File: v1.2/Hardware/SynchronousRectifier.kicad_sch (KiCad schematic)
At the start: 22 parts, among them J1 MAINS_IN, Q21 BC817, Q22 BC817, U1 4N39, U2 4N39

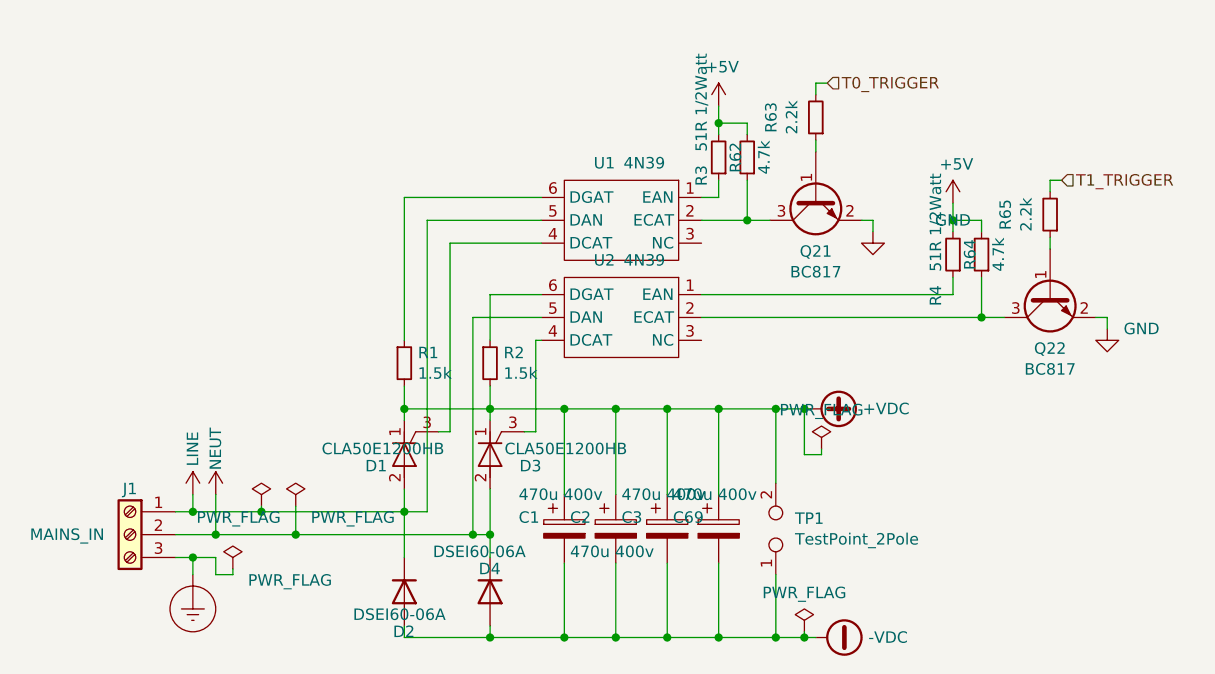
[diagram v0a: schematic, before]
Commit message: Addition of firmware to v1.2(not tested)
+Addition of power tracking(with duty cycle control).
+Addition of resonance freq tracking(via proprietary algorithm relied on active and reactive power measurements)
+Quality factor monitoring
+Power boost when loaded(idle and loaded modes)
+Much better frequency resolution(less than 1Hz)
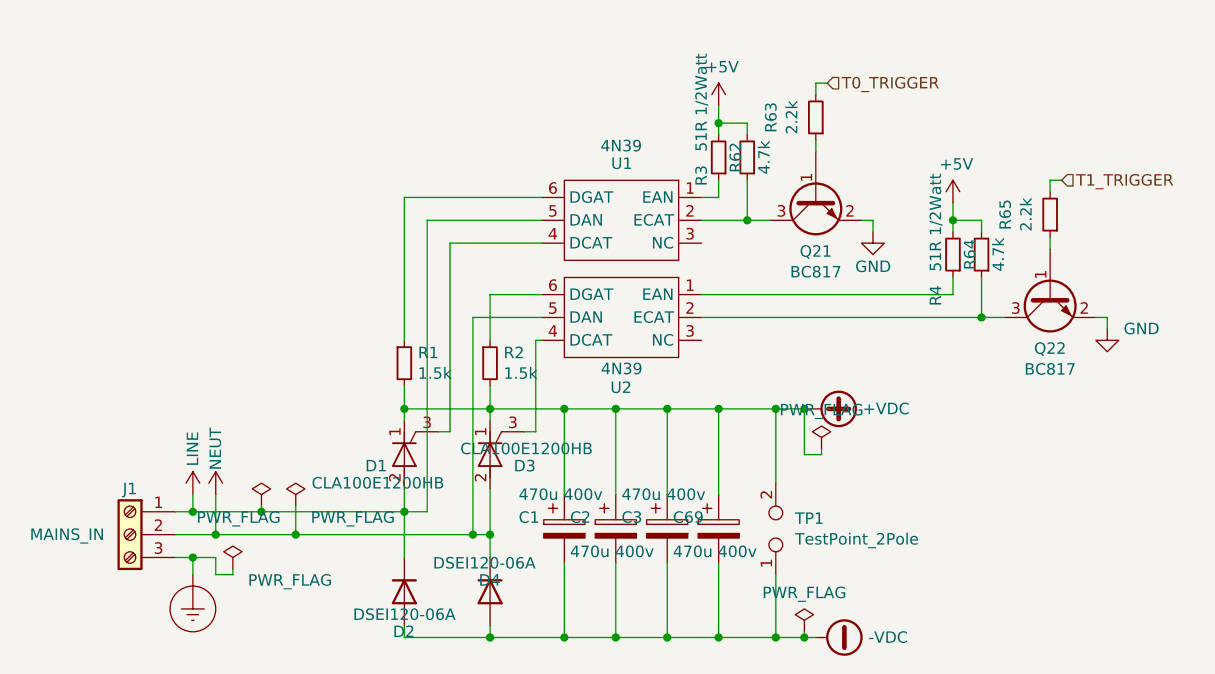
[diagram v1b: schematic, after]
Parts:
- D1, D3: value CLA50E1200HB -> CLA100E1200HB; Link https://ozdisan.com/power-semiconductors/thyristors/discret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 -> https://ozdisan.com/Product/Detail/458855/CLA100E1200HB; Price 13.43667TL -> 29.10196TL
- D2, D4: value DSEI60-06A -> DSEI120-06A; Link https://ozdisan.com/power-semiconductors/diodes-diode-modules-and-rectifiers/general-purpose-diodes/DSEI60-06A -> https://ozdisan.com/power-semiconductors/diodes-diode-modules-and-rectifiers/general-purpose-diodes/DSEI120-06A; Price 20.69234TL -> 47.67769

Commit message: Start of rs485 communication interface development.
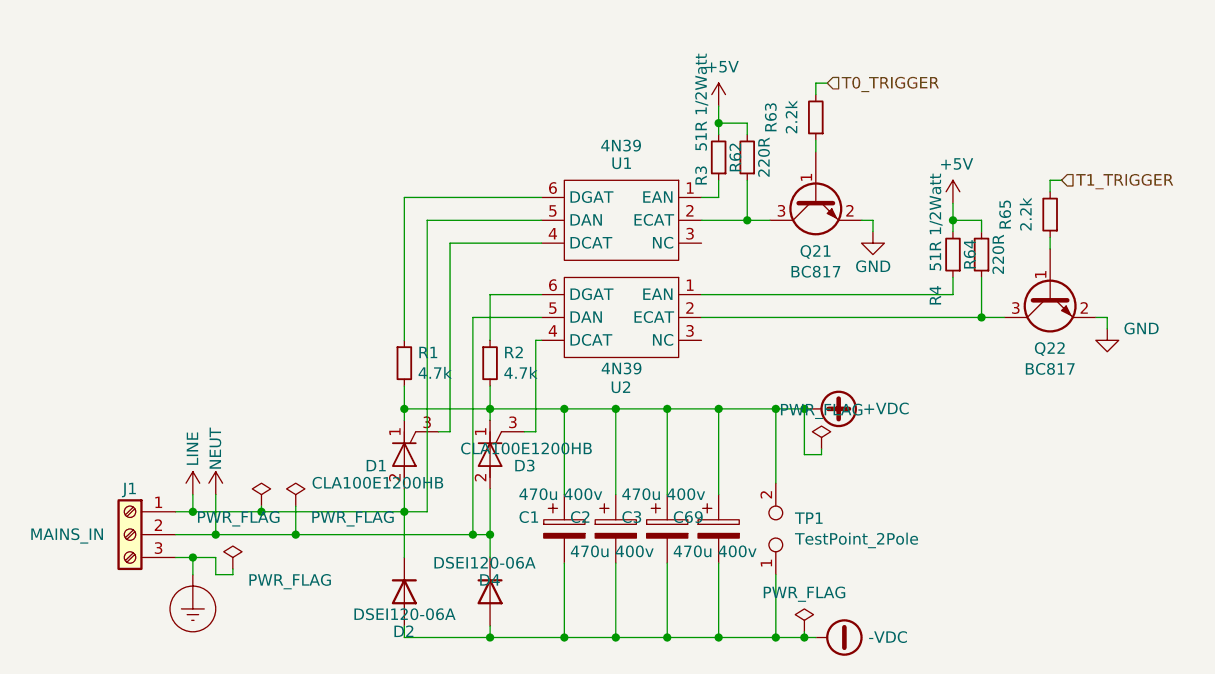
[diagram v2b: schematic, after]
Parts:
- R1, R2: value 1.5k -> 4.7k; Link https://ozdisan.com/passive-components/resistors/tht-through-hole-resistors/CFR0W8J0152A50 -> https://ozdisan.com/passive-components/resistors/tht-through-hole-resistors/CFR0W8J0472A50; Price 0.01961TL -> 0.0389TL
- R62, R64: value 4.7k -> 220R; Link https://ozdisan.com/passive-components/resistors/smt-smd-and-chip-resistors/0805S8F4701T5E -> https://ozdisan.com/passive-components/resistors/smt-smd-and-chip-resistors/0805S8J0221T5E; Price 0.01955TL -> 0.01498TL
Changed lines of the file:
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@@
 (kicad_sch (version 20200618) (host eeschema "5.99.0-unknown-f3f1740~101~ubuntu18.04.1")
-  (page 9 8)
+  (page 4 8)
   (paper "A4")
   (junction (at 99.06 106.68) (diameter 0) (color 0 0 0 0))
@@
     )
   )
-  (symbol (lib_name "Device:R_Small_3") (lib_id "Device:R_Small") (at 122.555 90.17 0)
+  (symbol (lib_name "Device:R_Small_9") (lib_id "Device:R_Small") (at 122.555 90.17 0)
     (in_bom yes) (on_board yes)
     (property "Reference" "R1" (id 0) (at 124.0536 89.027 0)
       (effects (font (size 1.27 1.27)) (justify left))
     )
-    (property "Value" "1.5k" (id 1) (at 124.0536 91.313 0)
+    (property "Value" "4.7k" (id 1) (at 124.0536 91.313 0)
       (effects (font (size 1.27 1.27)) (justify left))
     )
@@
       (effects (font (size 1.27 1.27)) hide)
     )
-    (property "Link" "https://ozdisan.com/passive-components/resistors/tht-through-hole-resistors/CFR0W8J0152A50" (id 4) (at 122.555 90.17 0)
-      (effects (font (size 1.27 1.27)) hide)
-    )
-    (property "Price" "0.01961TL" (id 5) (at 122.555 90.17 0)
-      (effects (font (size 1.27 1.27)) hide)
-    )
-  )
-  (symbol (lib_name "Device:R_Small_2") (lib_id "Device:R_Small") (at 132.08 90.17 0)
+    (property "Link" "https://ozdisan.com/passive-components/resistors/tht-through-hole-resistors/CFR0W8J0472A50" (id 4) (at 122.555 90.17 0)
+      (effects (font (size 1.27 1.27)) hide)
+    )
+    (property "Price" "0.0389TL" (id 5) (at 122.555 90.17 0)
+      (effects (font (size 1.27 1.27)) hide)
+    )
+  )
+  (symbol (lib_name "Device:R_Small_9") (lib_id "Device:R_Small") (at 132.08 90.17 0) (unit 1)
     (in_bom yes) (on_board yes)
     (property "Reference" "R2" (id 0) (at 133.5786 89.027 0)
       (effects (font (size 1.27 1.27)) (justify left))
     )
-    (property "Value" "1.5k" (id 1) (at 133.5786 91.313 0)
+    (property "Value" "4.7k" (id 1) (at 133.5786 91.313 0)
       (effects (font (size 1.27 1.27)) (justify left))
     )
@@
       (effects (font (size 1.27 1.27)) hide)
     )
-    (property "Link" "https://ozdisan.com/passive-components/resistors/tht-through-hole-resistors/CFR0W8J0152A50" (id 4) (at 132.08 90.17 0)
-      (effects (font (size 1.27 1.27)) hide)
-    )
-    (property "Price" "0.01961TL" (id 5) (at 132.08 90.17 0)
+    (property "Link" "https://ozdisan.com/passive-components/resistors/tht-through-hole-resistors/CFR0W8J0472A50" (id 4) (at 132.08 90.17 0)
+      (effects (font (size 1.27 1.27)) hide)
+    )
+    (property "Price" "0.0389TL" (id 5) (at 132.08 90.17 0)
       (effects (font (size 1.27 1.27)) hide)
     )
@@
     (in_bom yes) (on_board yes)
     (property "Reference" "R62" (id 0) (at 159.385 67.31 90))
-    (property "Value" "4.7k" (id 1) (at 162.56 67.31 90))
+    (property "Value" "220R" (id 1) (at 162.56 67.31 90))
     (property "Footprint" "Resistor_SMD:R_0805_2012Metric" (id 2) (at 160.655 67.31 0)
       (effects (font (size 1.27 1.27)) hide)
@@
       (effects (font (size 1.27 1.27)) hide)
     )
-    (property "Link" "https://ozdisan.com/passive-components/resistors/smt-smd-and-chip-resistors/0805S8F4701T5E" (id 4) (at 160.655 67.31 90)
-      (effects (font (size 1.27 1.27)) hide)
-    )
-    (property "Price" "0.01955TL" (id 5) (at 160.655 67.31 90)
+    (property "Link" "https://ozdisan.com/passive-components/resistors/smt-smd-and-chip-resistors/0805S8J0221T5E" (id 4) (at 160.655 67.31 90)
+      (effects (font (size 1.27 1.27)) hide)
+    )
+    (property "Price" "0.01498TL" (id 5) (at 160.655 67.31 90)
       (effects (font (size 1.27 1.27)) hide)
     )
@@
     (in_bom yes) (on_board yes)
     (property "Reference" "R64" (id 0) (at 185.42 78.105 90))
-    (property "Value" "4.7k" (id 1) (at 188.595 78.105 90))
+    (property "Value" "220R" (id 1) (at 188.595 78.105 90))
     (property "Footprint" "Resistor_SMD:R_0805_2012Metric" (id 2) (at 186.69 78.105 0)
       (effects (font (size 1.27 1.27)) hide)
@@
       (effects (font (size 1.27 1.27)) hide)
     )
-    (property "Link" "https://ozdisan.com/passive-components/resistors/smt-smd-and-chip-resistors/0805S8F4701T5E" (id 4) (at 186.69 78.105 90)
-      (effects (font (size 1.27 1.27)) hide)
-    )
-    (property "Price" "0.01955TL" (id 5) (at 186.69 78.105 90)
-      (effects (font (size 1.27 1.27)) hide)
-    )
+    (property "Link" "https://ozdisan.com/passive-components/resistors/smt-smd-and-chip-resistors/0805S8J0221T5E" (id 4) (at 186.69 78.105 90)
+      (effects (font (size 1.27 1.27)) hide)
+    )
+    (property "Price" "0.01498TL" (id 5) (at 186.69 78.105 90)
+      (effects (font (size 1.27 1.27)) hide)
+    )

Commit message: Redesign.
+Cli interface.
+Modularity improvement(complex number and pid modules created)
+Range change.
+Core-Lattice seperated. 
+Improvement of the control function
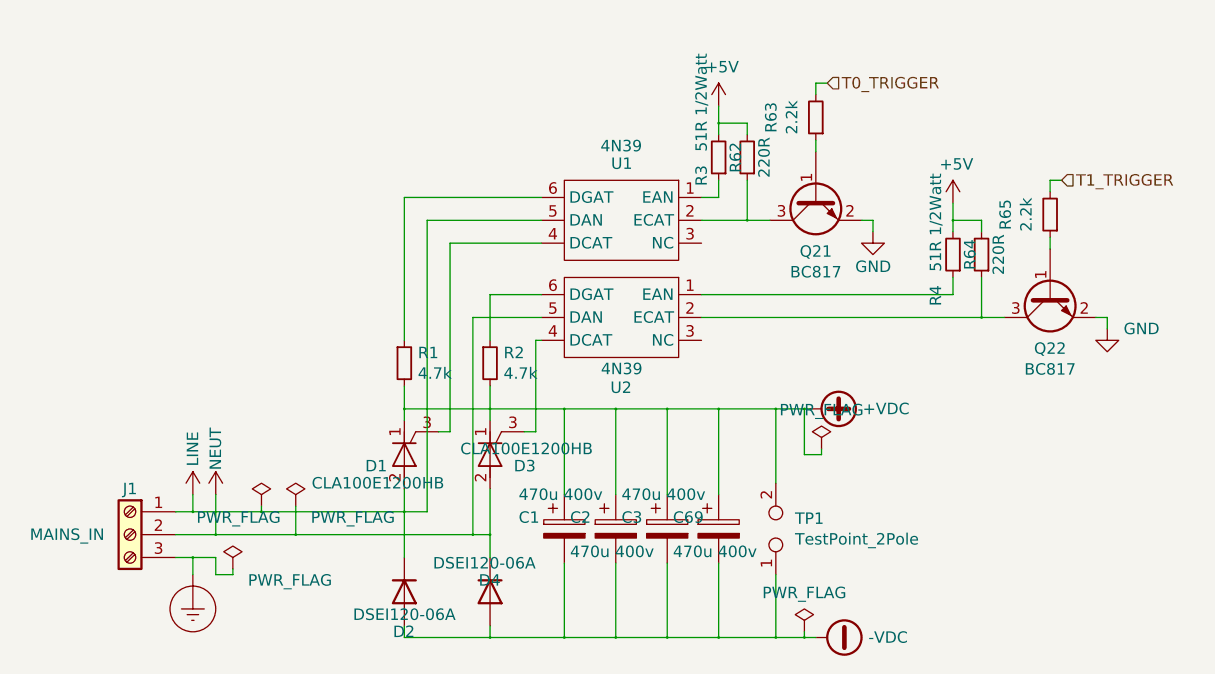
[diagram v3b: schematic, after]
